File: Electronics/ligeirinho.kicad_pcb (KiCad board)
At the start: 2 copper layers, 76.1 x 55.1 mm, 20 parts, among them J1 Bateria, J10 ponte H2, J11 VS1838B, J12 MPU6050, J13 ADNS-9500, J14 ADNS-9500 3V3, J2 ESP32 esq, J3 ESP32 dir, J4 VL53L0X 1, J5 VL53L0X 2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

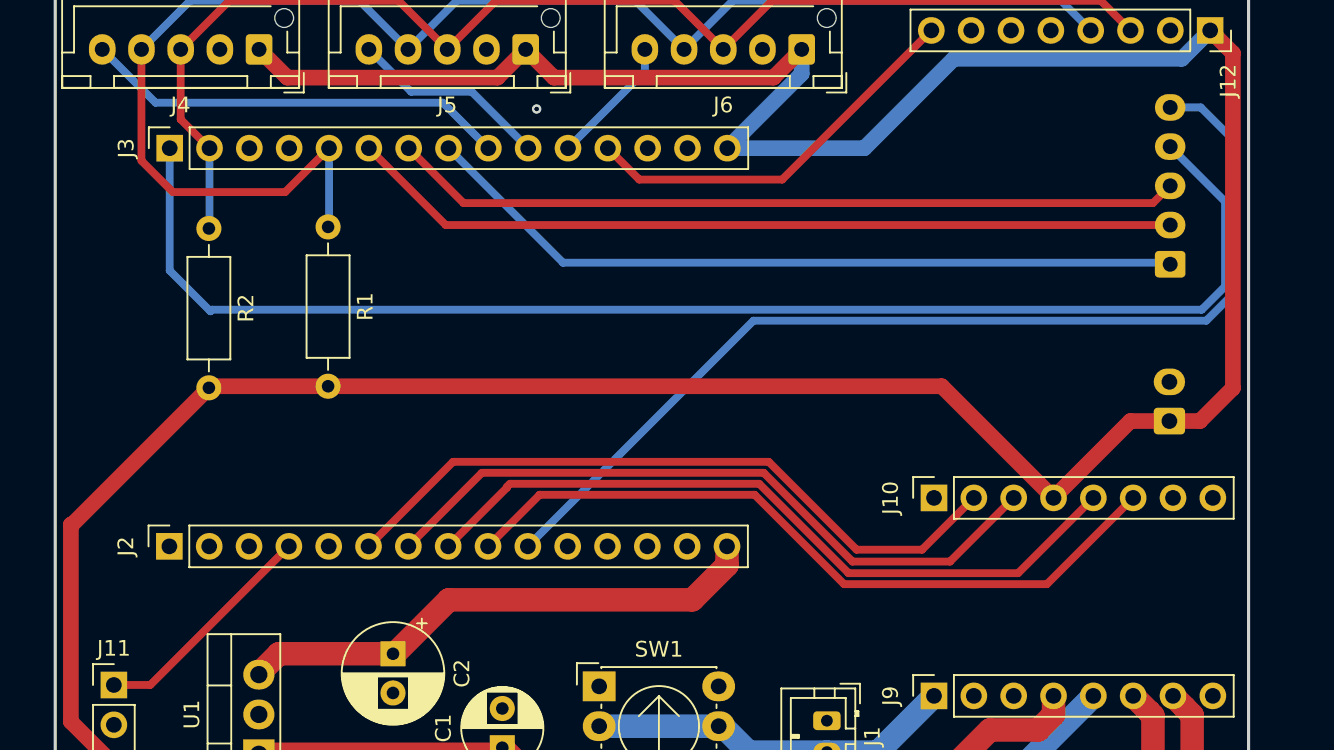
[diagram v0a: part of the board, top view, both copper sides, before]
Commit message: shore: add stickers
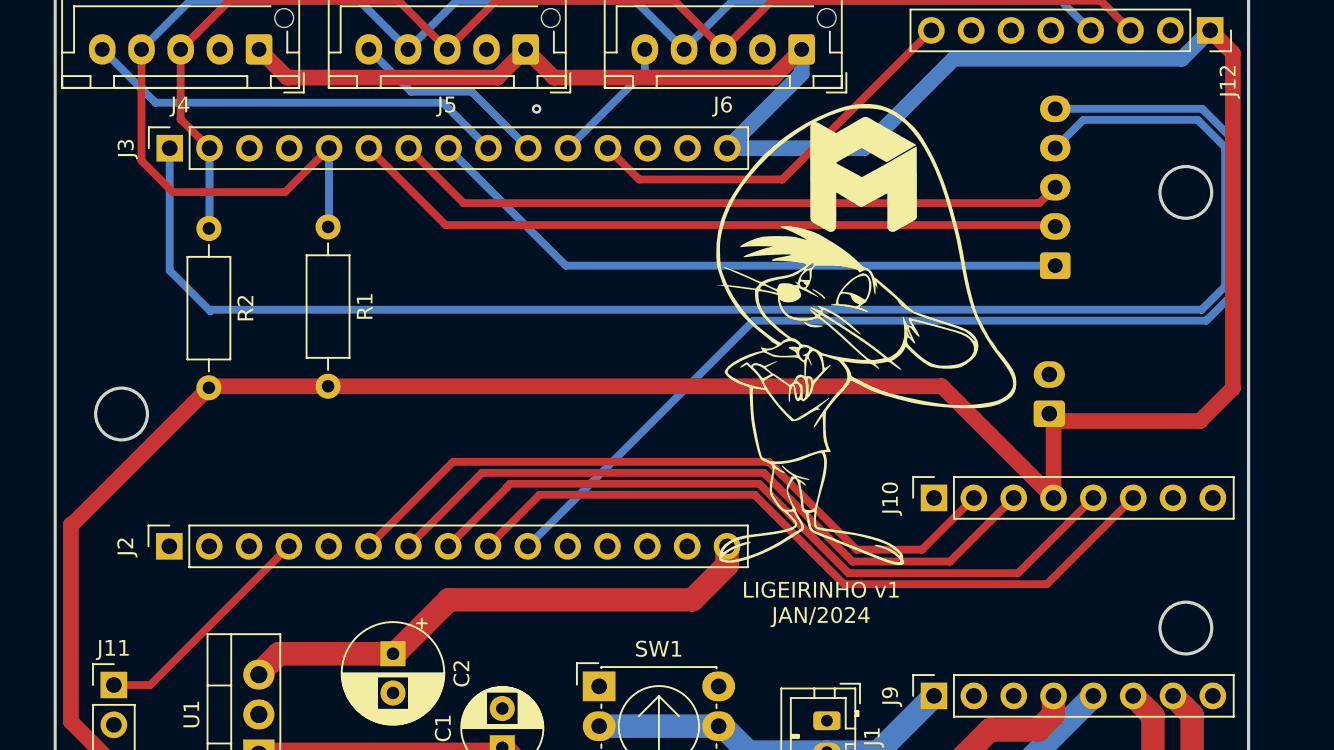
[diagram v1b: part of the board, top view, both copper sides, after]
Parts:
- added G***: LOGO, Logos:ligeirinho, F.Cu at (205.8, 108.2)
- added G***: LOGO, Logos:N-neon-logo-7mm, F.Cu at (205.9, 98.0)
- added G***: LOGO, Logos:neon-logo-vertical-50mm, B.Cu at (179.7, 109.8)
- added G***: LOGO, Logos:Camaneon-preto-e-branco-9mm, B.Cu at (226.1, 98.2)
- moved J14 7.67 mm to (217.8, 113.2)
- moved J13 7.33 mm to (218.2, 103.8)
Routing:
- net MOSI sm: track 87.2 -> 98.0 mm
- net sclk: track 50.5 -> 43.1 mm
- net motion: track 66.5 -> 73.8 mm
- net SS/CS: track 49.1 -> 41.8 mm
- net MISO sm: track 53.1 -> 45.8 mm
- net 3V3: track 203.2 -> 206.0 mm
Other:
- outline, holes or cut-outs redrawn
- board text added: "LIGEIRINHO v1 JAN/2024"

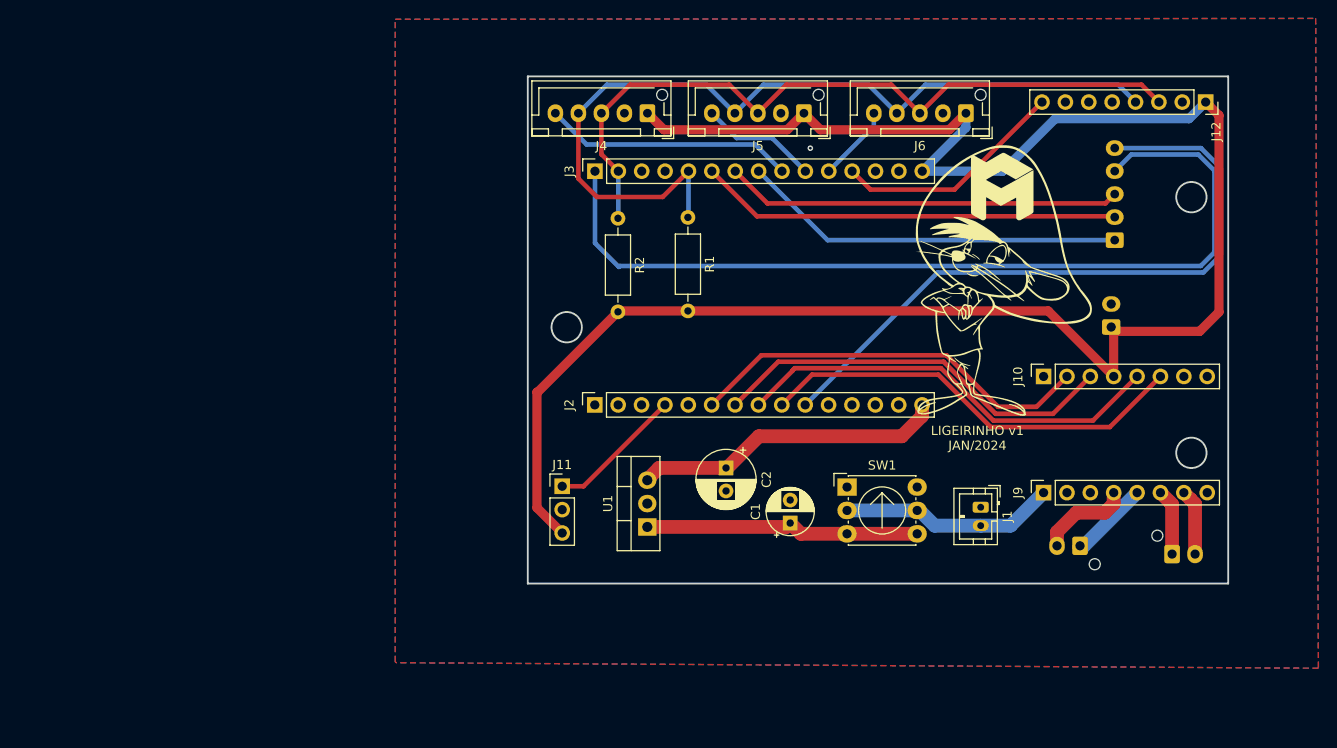
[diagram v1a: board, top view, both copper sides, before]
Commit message: shore: add measures
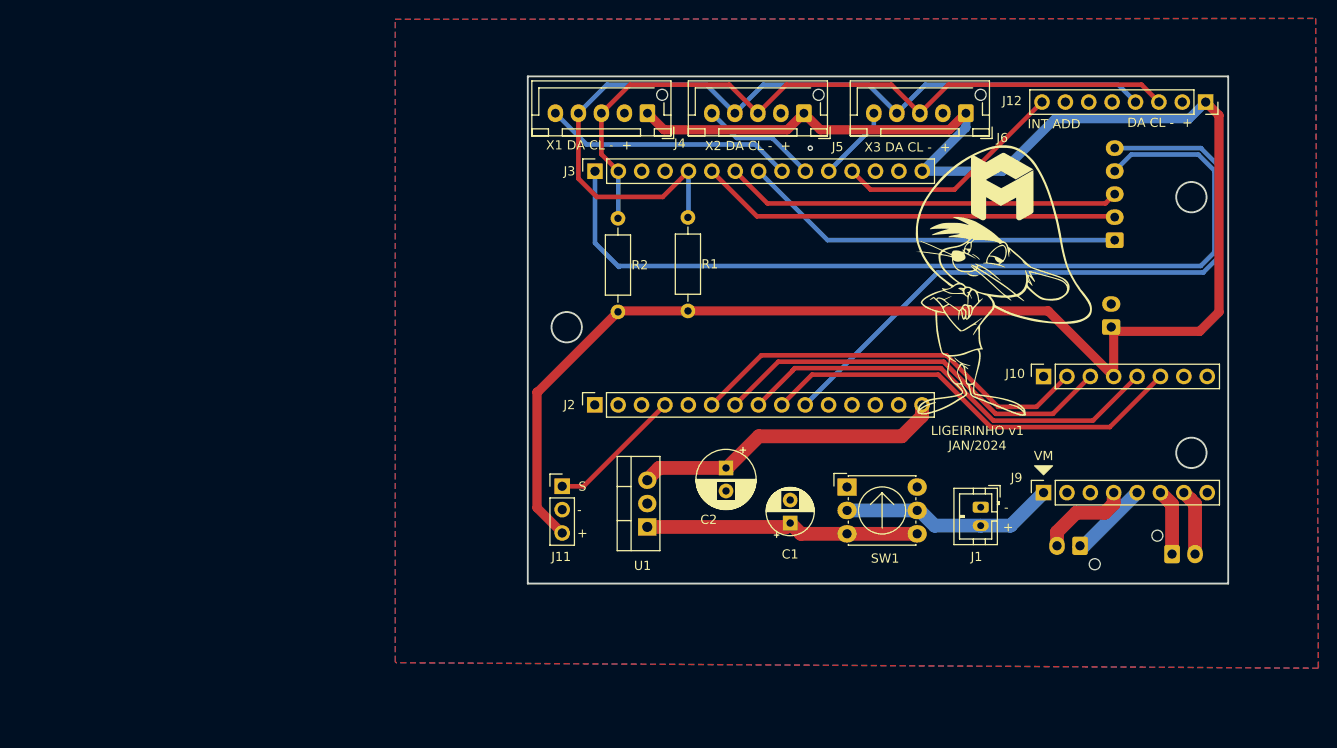
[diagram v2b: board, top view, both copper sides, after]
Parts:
- moved G*** 27.6 mm to (226.0, 125.8)
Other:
- board text added: "+"
- board text added: "-"
- board text added: "DA CL - +"
- board text added: "INT ADD"
- board text added: "MISO"
- board text added: "MOSI"
- board text added: "MOT"
- board text added: "NCS"
- board text added: "S"
- board text added: "SCLK"
- board text added: "VM"
- board text added: "X1 DA CL - +"
- board text added: "X2 DA CL - +"
- board text added: "X3 DA CL - +"

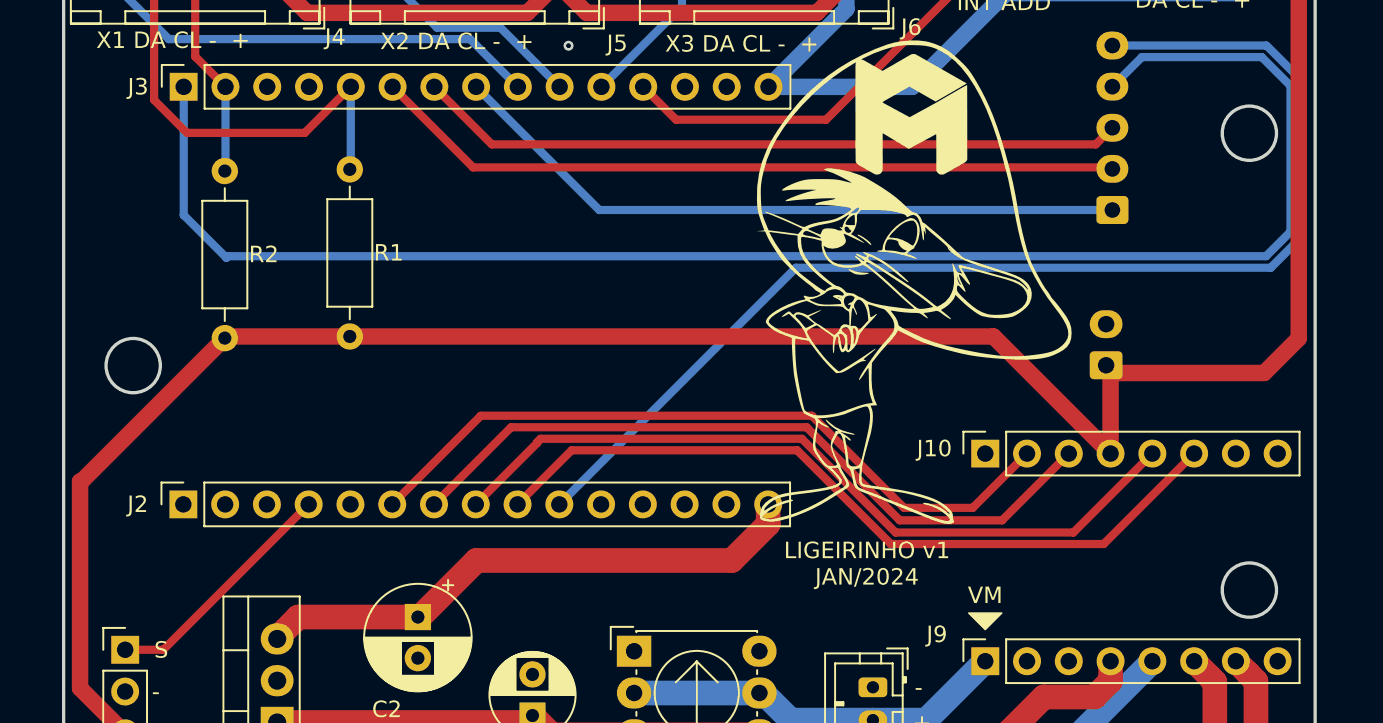
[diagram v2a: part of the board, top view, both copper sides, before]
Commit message: shore: add measures
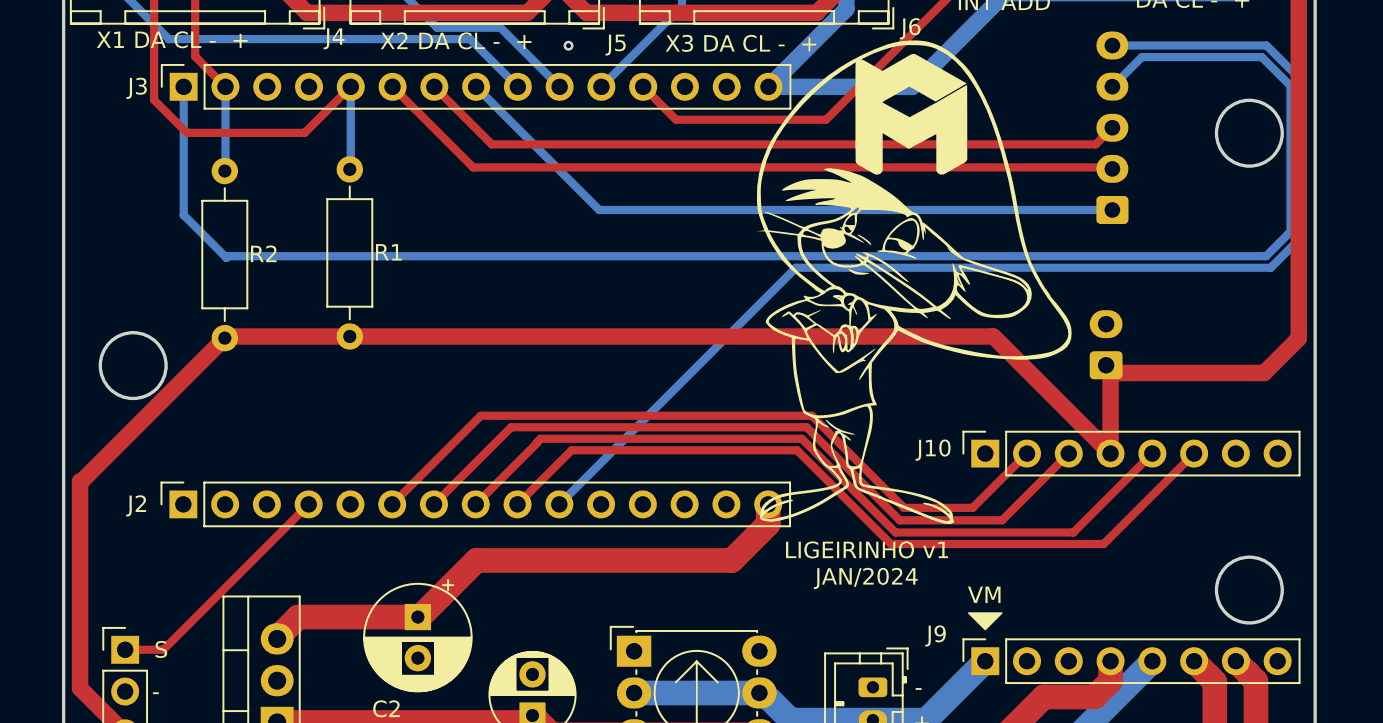
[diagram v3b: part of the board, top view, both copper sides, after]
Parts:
- moved G*** 0.47 mm to (226.4, 126.0)
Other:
- outline, holes or cut-outs redrawn
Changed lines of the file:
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@@
   )
   (footprint "Logos:Camaneon-preto-e-branco-9mm" (layer "B.Cu")
-    (at 226.03584 125.804556 180)
+    (at 226.44584 126.024556 180)
     (attr board_only exclude_from_pos_files exclude_from_bom)
     (fp_text reference "G***" (at 0 0) (layer "B.SilkS") hide
@@
   (gr_rect (start 154.4 86) (end 230.5 141.1)
     (stroke (width 0.2) (type default)) (fill none) (layer "Edge.Cuts"))
-  (gr_circle (center 158.63 113.25) (end 160.280757 113.25)
+  (gr_circle (center 158.63 113.25) (end 160.63 113.25)
     (stroke (width 0.2) (type default)) (fill none) (layer "Edge.Cuts"))
-  (gr_circle (center 226.5 99.12) (end 228.15 99.12)
+  (gr_circle (center 226.5 99.12) (end 228.5 99.12)
     (stroke (width 0.2) (type default)) (fill none) (layer "Edge.Cuts"))
-  (gr_circle (center 226.5 126.9) (end 228.15 126.9)
+  (gr_circle (center 226.5 126.9) (end 228.5 126.9)
     (stroke (width 0.2) (type default)) (fill none) (layer "Edge.Cuts"))
   (gr_rect (start 155.3 94.8) (end 207 123.2)

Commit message: fix(Electronics): add VIN tag to PCB
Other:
- board text added: "VIN"
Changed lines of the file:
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@@
+    )
+    (stroke (width 0.1) (type solid)) (fill solid) (layer "F.SilkS"))
+  (gr_poly
+    (pts
+      (xy 196.32 118.79)
+      (xy 198.32 118.79)
+      (xy 197.32 119.79)
     )
     (stroke (width 0.1) (type solid)) (fill solid) (layer "F.SilkS"))
@@
     (effects (font (size 1 1) (thickness 0.125)) (justify left bottom mirror))
   )
+  (gr_text "VIN" (at 196.04 118.65) (layer "F.SilkS")
+    (effects (font (size 1 1) (thickness 0.1)) (justify left bottom))
+  )
   (gr_text "X3 DA CL -  +" (at 190.97 94.28) (layer "F.SilkS")

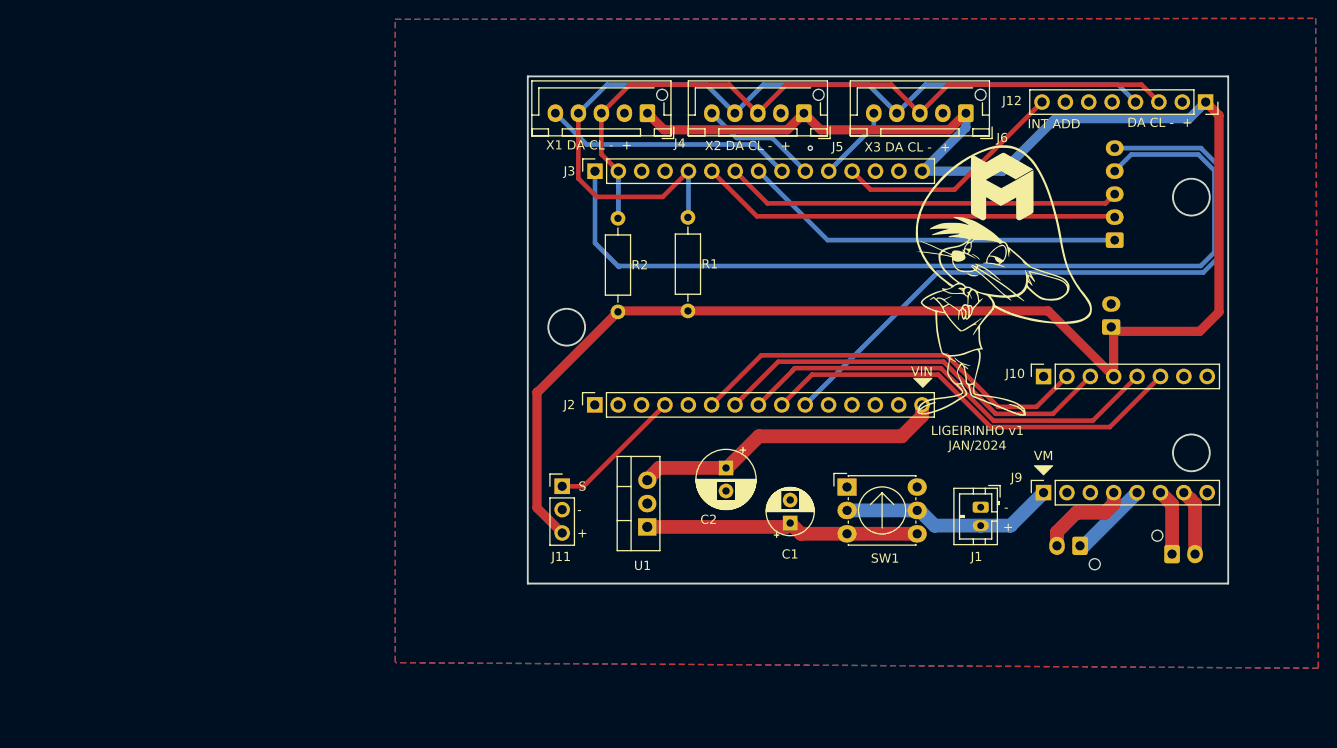
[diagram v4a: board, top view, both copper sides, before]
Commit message: fix: add 10uF capacitors and stitching
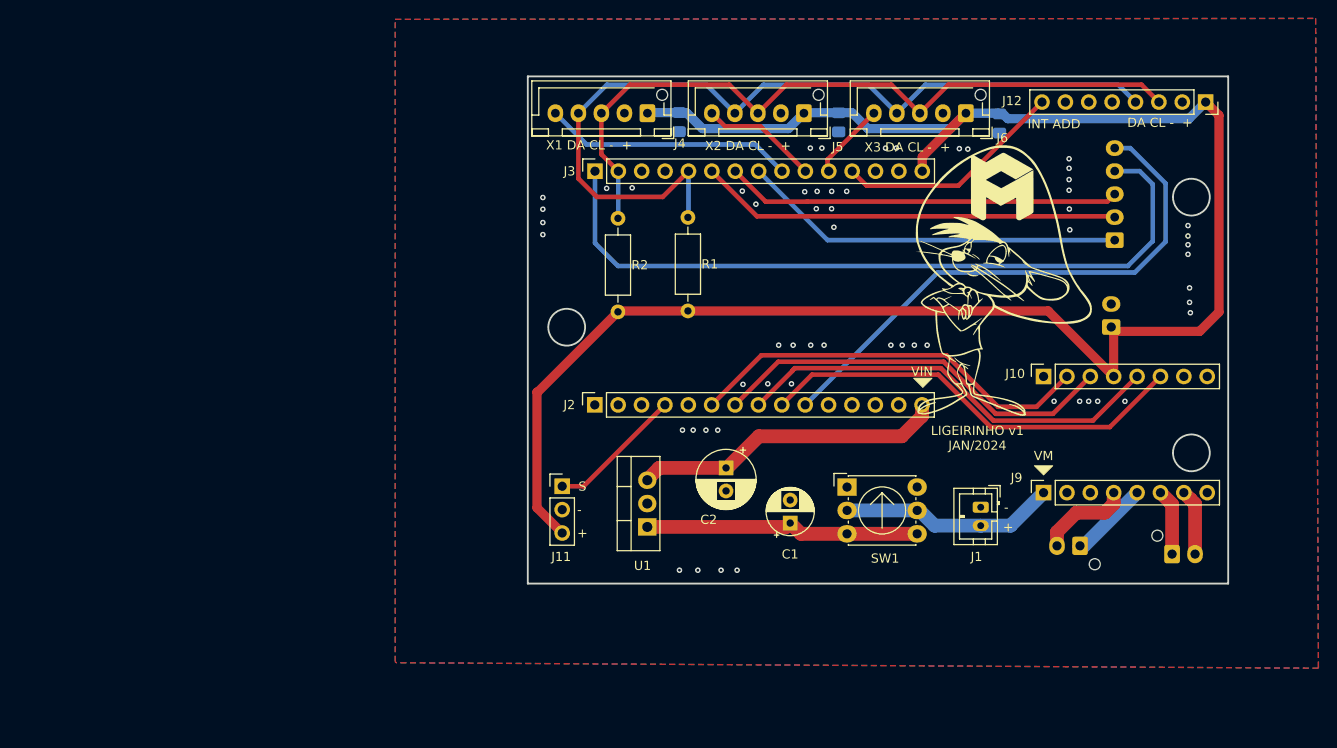
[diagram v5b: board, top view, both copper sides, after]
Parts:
- added C3: 10uf, Capacitor_SMD:C_0805_2012Metric_Pad1.18x1.45mm_HandSolder, B.Cu at (170.8, 91.0)
- added C4: 10uf, Capacitor_SMD:C_0805_2012Metric_Pad1.18x1.45mm_HandSolder, B.Cu at (188.2, 91.0)
- added C5: 10uf, Capacitor_SMD:C_0805_2012Metric_Pad1.18x1.45mm_HandSolder, B.Cu at (205.7, 91.1)
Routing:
- net MOSI sm: track 98.0 -> 81.5 mm
- net motion: track 73.8 -> 60.0 mm
- net 3V3: track 206.0 -> 199.0 mm
- net GND: vias 1 -> 56
- net (no net): vias 0 -> 2
